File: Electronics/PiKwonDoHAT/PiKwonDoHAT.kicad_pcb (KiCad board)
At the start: 2 copper layers, 43 x 57 mm, 42 parts, among them J1 RJ10, J2 RJ10, J3 RJ10, J4 RJ10, J5 Conn_02x20_Odd_Even, U1 74LV1T34, U2 74LV1T34, U3 74LV1T34, U4 74LV1T34

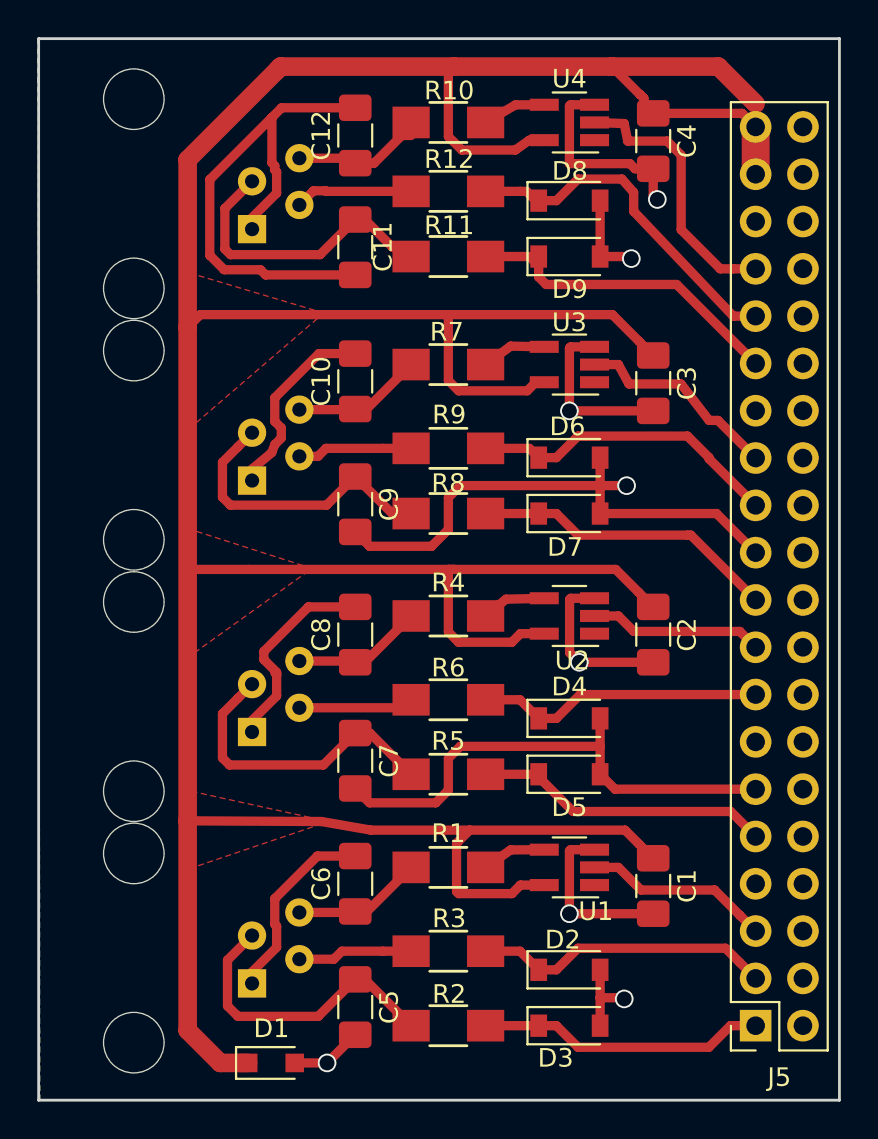
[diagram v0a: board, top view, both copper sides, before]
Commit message: Created bom and updated pcb
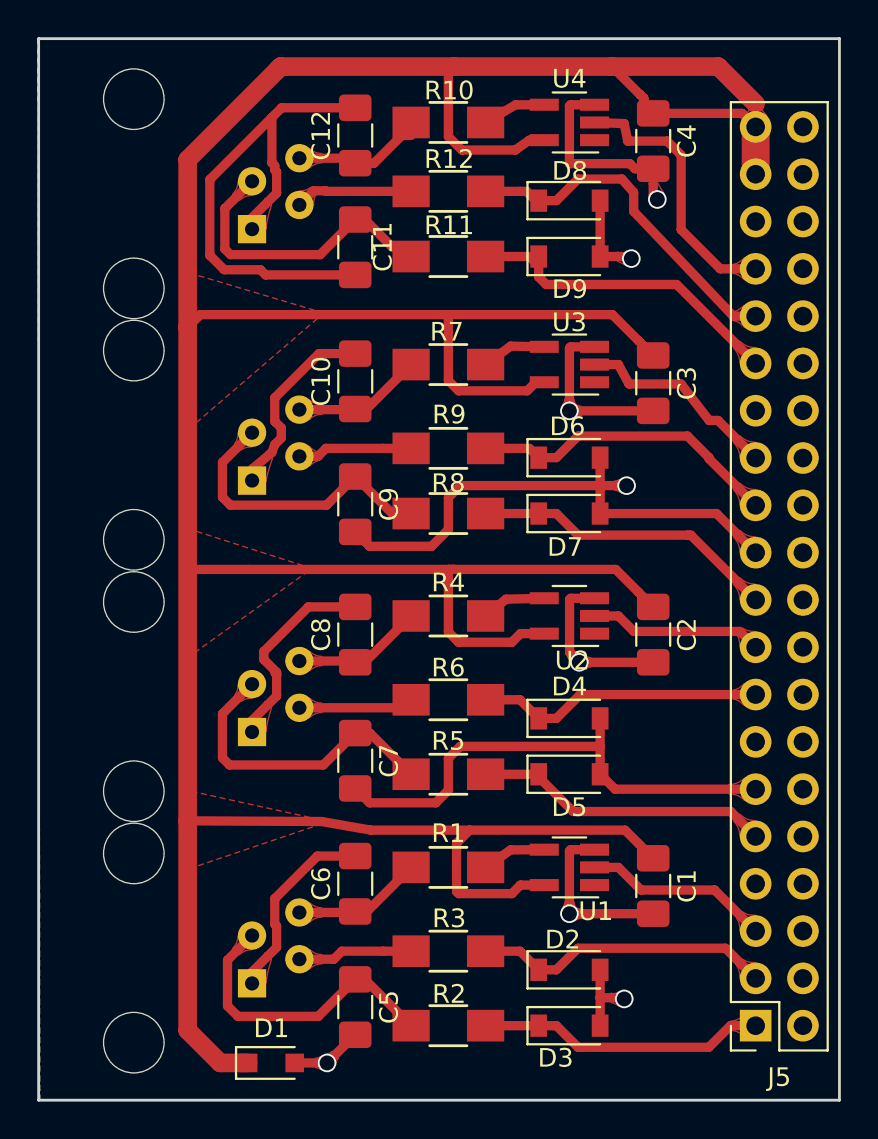
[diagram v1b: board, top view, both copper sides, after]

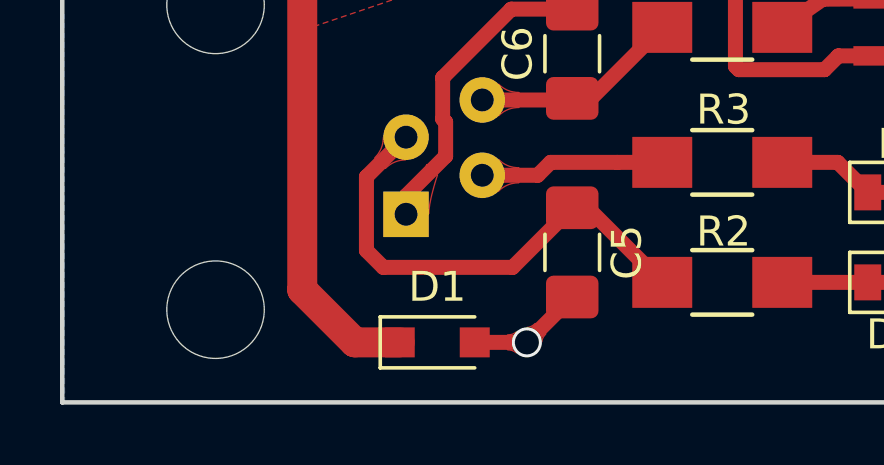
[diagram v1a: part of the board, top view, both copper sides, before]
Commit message: Updated diode footprint for improved solderability
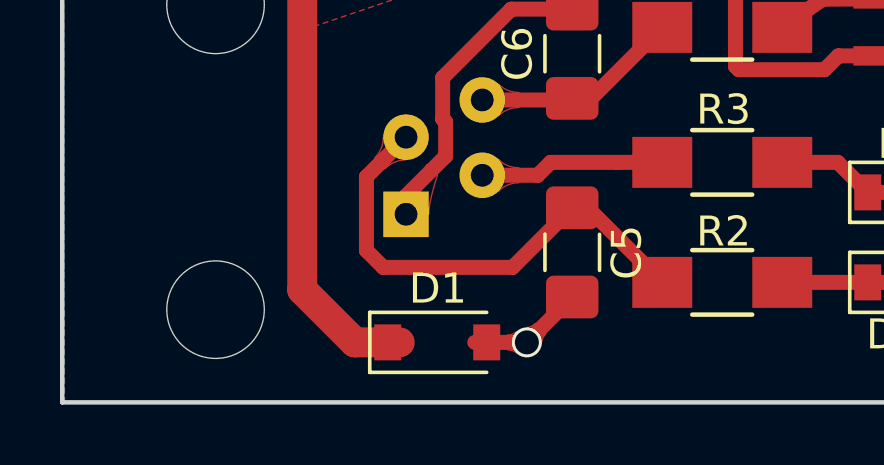
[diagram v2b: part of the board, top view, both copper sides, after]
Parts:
- D1: footprint Diodes_SMD:D_SOD-323_HandSoldering -> Diode_SMD:D_SOD-123
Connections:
- J5 pad 10: Net-(J5-Pad10) -> (no net)
- J5 pad 12: Net-(J5-Pad12) -> (no net)
- J5 pad 13: Net-(J5-Pad13) -> (no net)
- J5 pad 14: Net-(J5-Pad14) -> (no net)
- J5 pad 16: Net-(J5-Pad16) -> (no net)
- J5 pad 18: Net-(J5-Pad18) -> (no net)
- J5 pad 20: Net-(J5-Pad20) -> (no net)
- J5 pad 22: Net-(J5-Pad22) -> (no net)
- J5 pad 24: Net-(J5-Pad24) -> (no net)
- J5 pad 26: Net-(J5-Pad26) -> (no net)
- J5 pad 28: Net-(J5-Pad28) -> (no net)
- J5 pad 30: Net-(J5-Pad30) -> (no net)
- J5 pad 32: Net-(J5-Pad32) -> (no net)
- J5 pad 34: Net-(J5-Pad34) -> (no net)
- J5 pad 36: Net-(J5-Pad36) -> (no net)
- J5 pad 38: Net-(J5-Pad38) -> (no net)
- J5 pad 4: Net-(J5-Pad4) -> (no net)
- J5 pad 40: Net-(J5-Pad40) -> (no net)
- J5 pad 6: Net-(J5-Pad6) -> (no net)
- J5 pad 8: Net-(J5-Pad8) -> (no net)
- U1 pad 1: Net-(U1-Pad1) -> (no net)
- U2 pad 1: Net-(U2-Pad1) -> (no net)
- U3 pad 1: Net-(U3-Pad1) -> (no net)
- U4 pad 1: Net-(U4-Pad1) -> (no net)
